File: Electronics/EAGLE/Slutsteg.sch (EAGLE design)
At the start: 151 parts, among them CN1 OSTYK33102030-2, CN2 OSTYK33102030-2, CN3 OSTYK33102030-2, CN4 OSTYK33102030-2, IC1 SPX1117M3-L-3-3_TR, IC10 LM324D, IC11 L78M12ABDT-TR, IC3 ESP32-WROVER-IE-4MB, IC4 TM8211, IC6 TPA3244DDWR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

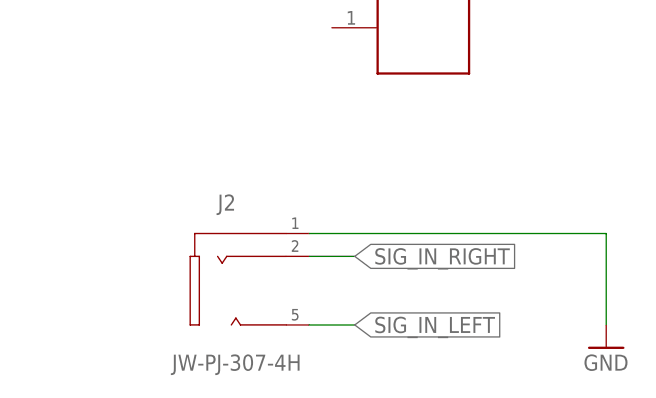
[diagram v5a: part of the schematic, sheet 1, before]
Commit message: Revert "Lagt till 3.5mm connector"
This reverts commit b586c7d4102b99b6a6c1c70b6fd3026c9e3e15a7.
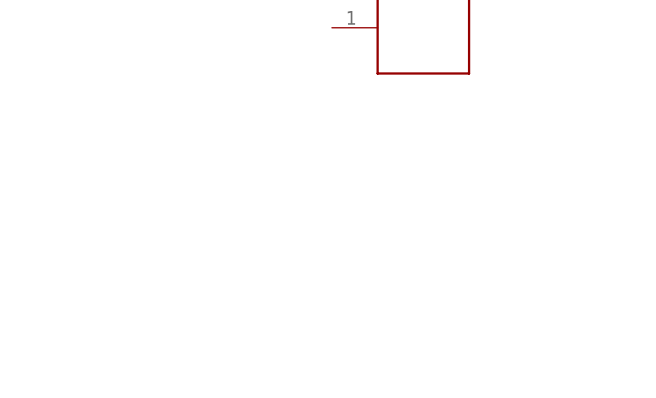
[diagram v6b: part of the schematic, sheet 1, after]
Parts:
- removed J2: JW-PJ-307-4H, jack_04:JW-PJ-307-4H
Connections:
- net GND: no longer J2.1
- net SIG_IN_LEFT: no longer J2.5
- net SIG_IN_RIGHT: no longer J2.2
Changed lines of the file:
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@@
 <part name="C78" library="rcl" library_urn="urn:adsk.eagle:library:334" deviceset="C-EU" device="C0805" package3d_urn="urn:adsk.eagle:package:23617/2" value="1uF/50V"/>
 <part name="C79" library="rcl" library_urn="urn:adsk.eagle:library:334" deviceset="C-EU" device="C0805" package3d_urn="urn:adsk.eagle:package:23617/2" value="1uF/50V"/>
-<part name="J2" library="jack_04" deviceset="JW-PJ-307-4" device="H"/>
-<part name="GND10" library="supply1" library_urn="urn:adsk.eagle:library:371" deviceset="GND" device=""/>
 </parts>
 <sheets>
@@
 <attribute name="VALUE" x="99.06" y="154.94" size="1.778" layer="96"/>
 </instance>
-<instance part="J2" gate="G$1" x="327.66" y="99.06" smashed="yes">
-<attribute name="NAME" x="325.12" y="106.68" size="1.778" layer="95"/>
-<attribute name="VALUE" x="320.04" y="88.9" size="1.778" layer="96"/>
-</instance>
-<instance part="GND10" gate="1" x="368.3" y="91.44" smashed="yes">
-<attribute name="VALUE" x="365.76" y="88.9" size="1.778" layer="96"/>
-</instance>
 </instances>
 <busses>
@@
 <wire x1="101.6" y1="160.02" x2="101.6" y2="198.12" width="0.1524" layer="91"/>
 <wire x1="101.6" y1="198.12" x2="111.76" y2="198.12" width="0.1524" layer="91"/>
-</segment>
-<segment>
-<pinref part="GND10" gate="1" pin="GND"/>
-<pinref part="J2" gate="G$1" pin="1"/>
-<wire x1="368.3" y1="93.98" x2="368.3" y2="104.14" width="0.1524" layer="91"/>
-<wire x1="368.3" y1="104.14" x2="335.28" y2="104.14" width="0.1524" layer="91"/>
 </segment>
 </net>
@@
 </segment>
 </net>
-<net name="SIG_IN_RIGHT" class="0">
-<segment>
-<pinref part="J2" gate="G$1" pin="2"/>
-<wire x1="335.28" y1="101.6" x2="340.36" y2="101.6" width="0.1524" layer="91"/>
-<label x="340.36" y="101.6" size="1.778" layer="95" xref="yes"/>
-</segment>
-</net>
-<net name="SIG_IN_LEFT" class="0">
-<segment>
-<pinref part="J2" gate="G$1" pin="5"/>
-<wire x1="335.28" y1="93.98" x2="340.36" y2="93.98" width="0.1524" layer="91"/>
-<label x="340.36" y="93.98" size="1.778" layer="95" xref="yes"/>
-</segment>
-</net>

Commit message: Changed components
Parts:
- C18: value ECA-1HM471B -> 16PK470MEFC8X11.5; device SamacSys_Parts:ECA-1HM471B -> SamacSys_Parts:16PK470MEFC8X11.5
- C30, C31: device SamacSys_Parts:ECA-1HM471B -> SamacSys_Parts:UVY1H102MHD
- C47: device TPA3244.dbl:SAMACSYS_PARTS_ECA-1HM471B -> SamacSys_Parts:16PK470MEFC8X11.5
- C63, C64: device TPA3244.dbl:SAMACSYS_PARTS_ECA-1HM471B -> SamacSys_Parts:UVY1H102MHD
- L1, L2, L3, L4: value 74477010 -> 48100SC; device SamacSys_Parts:74477010 -> SamacSys_Parts:48100SC
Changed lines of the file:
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@@
 <part name="FRAME1" library="frames" library_urn="urn:adsk.eagle:library:229" deviceset="A3L-LOC" device=""/>
 <part name="IC7" library="SamacSys_Parts" deviceset="TPA3251D2DDVR" device=""/>
-<part name="C63" library="TPA3244.dbl" deviceset="SAMACSYS_PARTS_ECA-1HM471B" device="" value="ECA-1HM102B"/>
-<part name="C64" library="TPA3244.dbl" deviceset="SAMACSYS_PARTS_ECA-1HM471B" device="" value="ECA-1HM102B"/>
+<part name="C63" library="SamacSys_Parts" deviceset="UVY1H102MHD" device="" value="ECA-1HM102B"/>
+<part name="C64" library="SamacSys_Parts" deviceset="UVY1H102MHD" device="" value="ECA-1HM102B"/>
 <part name="L5" library="SamacSys_Parts" deviceset="74477010" device=""/>
 <part name="L6" library="SamacSys_Parts" deviceset="74477010" device=""/>
@@
 <part name="C59" library="rcl" library_urn="urn:adsk.eagle:library:334" deviceset="C-EU" device="C0805" package3d_urn="urn:adsk.eagle:package:23617/2" value="1uF/50V"/>
 <part name="C52" library="rcl" library_urn="urn:adsk.eagle:library:334" deviceset="C-EU" device="C0603" package3d_urn="urn:adsk.eagle:package:23616/2" value="100nF/50V"/>
-<part name="C47" library="TPA3244.dbl" deviceset="SAMACSYS_PARTS_ECA-1HM471B" device="" value="ECA-1HM471B"/>
+<part name="C47" library="SamacSys_Parts" deviceset="16PK470MEFC8X11.5" device="" value="ECA-1HM471B"/>
 <part name="C53" library="rcl" library_urn="urn:adsk.eagle:library:334" deviceset="C-EU" device="C0603" package3d_urn="urn:adsk.eagle:package:23616/2" value="100nF/50V"/>
 <part name="C51" library="rcl" library_urn="urn:adsk.eagle:library:334" deviceset="C-EU" device="C0603" package3d_urn="urn:adsk.eagle:package:23616/2" value="100nF/50V"/>
@@
 <part name="C44" library="rcl" library_urn="urn:adsk.eagle:library:334" deviceset="C-EU" device="C0603" package3d_urn="urn:adsk.eagle:package:23616/2" value="10nF/50V"/>
 <part name="R22" library="rcl" library_urn="urn:adsk.eagle:library:334" deviceset="R-EU_" device="R0603" package3d_urn="urn:adsk.eagle:package:23555/3" value="3.3R/5%/0.1W"/>
-<part name="C31" library="SamacSys_Parts" deviceset="ECA-1HM471B" device="" override_package3d_urn="urn:adsk.eagle:package:27155028/2" override_package_urn="urn:adsk.eagle:footprint:27155054/1" value="ECA-1HM102B"/>
-<part name="C30" library="SamacSys_Parts" deviceset="ECA-1HM471B" device="" override_package3d_urn="urn:adsk.eagle:package:27154914/2" override_package_urn="urn:adsk.eagle:footprint:27154916/1" value="ECA-1HM102B"/>
+<part name="C31" library="SamacSys_Parts" deviceset="UVY1H102MHD" device="" override_package3d_urn="urn:adsk.eagle:package:27155028/2" override_package_urn="urn:adsk.eagle:footprint:27155054/1" override_locally_modified="yes" value="ECA-1HM102B"/>
+<part name="C30" library="SamacSys_Parts" deviceset="UVY1H102MHD" device="" override_package3d_urn="urn:adsk.eagle:package:27154914/2" override_package_urn="urn:adsk.eagle:footprint:27154916/1" override_locally_modified="yes" value="ECA-1HM102B"/>
 <part name="R17" library="rcl" library_urn="urn:adsk.eagle:library:334" deviceset="R-EU_" device="R0603" package3d_urn="urn:adsk.eagle:package:23555/3" value="20K/5%/0.1W"/>
 <part name="C16" library="rcl" library_urn="urn:adsk.eagle:library:334" deviceset="C-EU" device="C0603" package3d_urn="urn:adsk.eagle:package:23616/2" value="100nF/50V"/>
@@
 <part name="C26" library="rcl" library_urn="urn:adsk.eagle:library:334" deviceset="C-EU" device="C0603" package3d_urn="urn:adsk.eagle:package:23616/2" value="100nF/50V"/>
 <part name="R18" library="rcl" library_urn="urn:adsk.eagle:library:334" deviceset="R-EU_" device="R0603" package3d_urn="urn:adsk.eagle:package:23555/3" value="3.3R/5%/0.1W"/>
-<part name="C18" library="SamacSys_Parts" deviceset="ECA-1HM471B" device="" override_package3d_urn="urn:adsk.eagle:package:27158126/2" override_package_urn="urn:adsk.eagle:footprint:27158127/1"/>
+<part name="C18" library="SamacSys_Parts" deviceset="16PK470MEFC8X11.5" device="" override_package3d_urn="urn:adsk.eagle:package:27158126/2" override_package_urn="urn:adsk.eagle:footprint:27158127/1" override_locally_modified="yes"/>
 <part name="C19" library="rcl" library_urn="urn:adsk.eagle:library:334" deviceset="C-EU" device="C0603" package3d_urn="urn:adsk.eagle:package:23616/2" value="100nF/50V"/>
 <part name="R16" library="rcl" library_urn="urn:adsk.eagle:library:334" deviceset="R-EU_" device="R0603" package3d_urn="urn:adsk.eagle:package:23555/3" value="20K/5%/0.1W"/>
@@
 <part name="R12" library="rcl" library_urn="urn:adsk.eagle:library:334" deviceset="R-EU_" device="R0603" package3d_urn="urn:adsk.eagle:package:23555/3" value="20K/5%/0.1W"/>
 <part name="+3V8" library="supply1" library_urn="urn:adsk.eagle:library:371" deviceset="+3V3" device=""/>
-<part name="L1" library="SamacSys_Parts" deviceset="74477010" device="" override_package3d_urn="urn:adsk.eagle:package:27154887/2" override_package_urn="urn:adsk.eagle:footprint:27154892/1"/>
-<part name="L2" library="SamacSys_Parts" deviceset="74477010" device="" override_package3d_urn="urn:adsk.eagle:package:27154899/2" override_package_urn="urn:adsk.eagle:footprint:27154900/1"/>
-<part name="L3" library="SamacSys_Parts" deviceset="74477010" device="" override_package3d_urn="urn:adsk.eagle:package:27154902/2" override_package_urn="urn:adsk.eagle:footprint:27154903/1"/>
-<part name="L4" library="SamacSys_Parts" deviceset="74477010" device="" override_package3d_urn="urn:adsk.eagle:package:27154904/2" override_package_urn="urn:adsk.eagle:footprint:27154905/1"/>
+<part name="L1" library="SamacSys_Parts" deviceset="48100SC" device="" override_package3d_urn="urn:adsk.eagle:package:27154887/2" override_package_urn="urn:adsk.eagle:footprint:27154892/1" override_locally_modified="yes"/>
+<part name="L2" library="SamacSys_Parts" deviceset="48100SC" device="" override_package3d_urn="urn:adsk.eagle:package:27154899/2" override_package_urn="urn:adsk.eagle:footprint:27154900/1" override_locally_modified="yes"/>
+<part name="L3" library="SamacSys_Parts" deviceset="48100SC" device="" override_package3d_urn="urn:adsk.eagle:package:27154902/2" override_package_urn="urn:adsk.eagle:footprint:27154903/1" override_locally_modified="yes"/>
+<part name="L4" library="SamacSys_Parts" deviceset="48100SC" device="" override_package3d_urn="urn:adsk.eagle:package:27154904/2" override_package_urn="urn:adsk.eagle:footprint:27154905/1" override_locally_modified="yes"/>
 <part name="C20" library="rcl" library_urn="urn:adsk.eagle:library:334" deviceset="C-EU" device="C0805" package3d_urn="urn:adsk.eagle:package:23617/2" value="1uF/50V"/>
 <part name="C23" library="rcl" library_urn="urn:adsk.eagle:library:334" deviceset="C-EU" device="C0805" package3d_urn="urn:adsk.eagle:package:23617/2" value="1uF/50V"/>
@@
 <segment>
 <pinref part="IC6" gate="G$1" pin="!RESET"/>
-<wire x1="152.4" y1="162.56" x2="71.12" y2="162.56" width="0.1524" layer="91"/>
+<wire x1="152.4" y1="162.56" x2="76.2" y2="162.56" width="0.1524" layer="91"/>
 <label x="71.12" y="162.56" size="0.8128" layer="95" rot="R180" xref="yes"/>
 <pinref part="R12" gate="G$1" pin="1"/>
-<wire x1="76.2" y1="175.26" x2="71.12" y2="162.56" width="0.1524" layer="91"/>
-<junction x="71.12" y="162.56"/>
-</segment>
-</net>
+<wire x1="76.2" y1="175.26" x2="76.2" y2="162.56" width="0.1524" layer="91"/>
+<junction x="76.2" y="162.56"/>
+<wire x1="76.2" y1="162.56" x2="71.12" y2="162.56" width="0.1524" layer="91"/>
+</segment>
+</net>

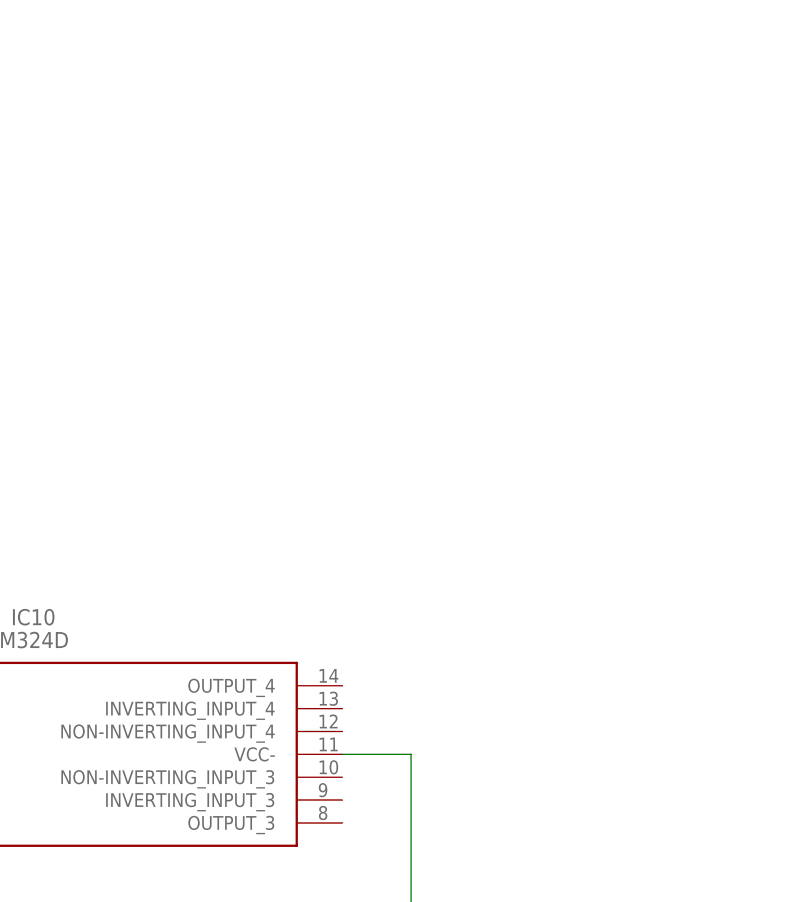
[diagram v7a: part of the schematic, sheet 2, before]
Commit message: Lagt till 3.5mm input och vridpot för Basen
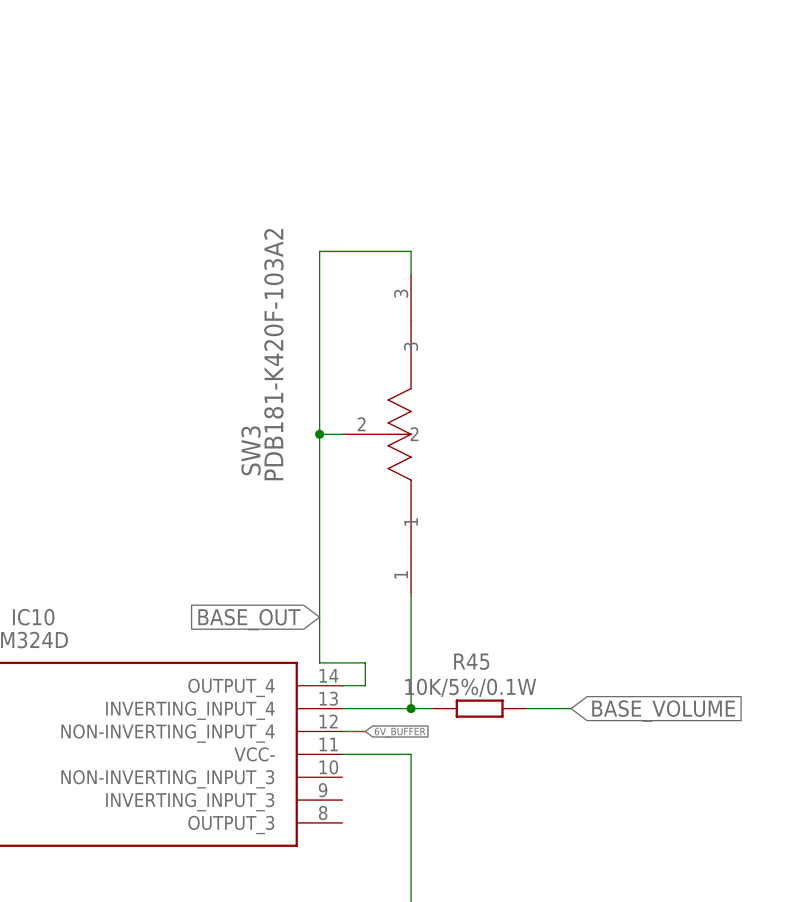
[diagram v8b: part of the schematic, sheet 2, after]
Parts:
- added J2: JW-PJ-307-4H, jack_04:JW-PJ-307-4H
- added R45: 10K/5%/0.1W, rcl:R-EU_R0603
- added SW3: PDB181-K420F-103A2, PDB181-K420F-103A2:PDB181-K420F-103A2
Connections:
- new net N$4: IC10.INVERTING_INPUT_4, R45.2, SW3.1
- net 6V_BUFFER: now also IC10.NON-INVERTING_INPUT_4
- net BASE_OUT: now also IC10.OUTPUT_4, SW3.2, SW3.3; no longer C75.1, R33.1
- net BASE_VOLUME: now also C75.1, R33.1, R45.1
- net GND: now also J2.1
- net SIG_IN_LEFT: now also J2.5
- net SIG_IN_RIGHT: now also J2.2
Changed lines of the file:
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@@
 <part name="C78" library="rcl" library_urn="urn:adsk.eagle:library:334" deviceset="C-EU" device="C0805" package3d_urn="urn:adsk.eagle:package:23617/2" value="1uF/50V"/>
 <part name="C79" library="rcl" library_urn="urn:adsk.eagle:library:334" deviceset="C-EU" device="C0805" package3d_urn="urn:adsk.eagle:package:23617/2" value="1uF/50V"/>
+<part name="J2" library="jack_04" deviceset="JW-PJ-307-4" device="H"/>
+<part name="GND10" library="supply1" library_urn="urn:adsk.eagle:library:371" deviceset="GND" device=""/>
+<part name="SW3" library="PDB181-K420F-103A2" deviceset="PDB181-K420F-103A2" device=""/>
+<part name="R45" library="rcl" library_urn="urn:adsk.eagle:library:334" deviceset="R-EU_" device="R0603" package3d_urn="urn:adsk.eagle:package:23555/3" value="10K/5%/0.1W"/>
 </parts>
 <sheets>
@@
 <attribute name="VALUE" x="99.06" y="154.94" size="1.778" layer="96"/>
 </instance>
+<instance part="J2" gate="G$1" x="325.12" y="68.58" smashed="yes">
+<attribute name="NAME" x="322.58" y="76.2" size="1.778" layer="95"/>
+<attribute name="VALUE" x="317.5" y="58.42" size="1.778" layer="96"/>
+</instance>
+<instance part="GND10" gate="1" x="365.76" y="60.96" smashed="yes">
+<attribute name="VALUE" x="363.22" y="58.42" size="1.778" layer="96"/>
+</instance>
 </instances>
 <busses>
@@
 <wire x1="101.6" y1="160.02" x2="101.6" y2="198.12" width="0.1524" layer="91"/>
 <wire x1="101.6" y1="198.12" x2="111.76" y2="198.12" width="0.1524" layer="91"/>
+</segment>
+<segment>
+<pinref part="GND10" gate="1" pin="GND"/>
+<pinref part="J2" gate="G$1" pin="1"/>
+<wire x1="365.76" y1="63.5" x2="365.76" y2="73.66" width="0.1524" layer="91"/>
+<wire x1="365.76" y1="73.66" x2="332.74" y2="73.66" width="0.1524" layer="91"/>
 </segment>
 </net>
@@
 <wire x1="149.86" y1="198.12" x2="154.94" y2="198.12" width="0.1524" layer="91"/>
 <junction x="149.86" y="198.12"/>
+</segment>
+</net>
+<net name="SIG_IN_RIGHT" class="0">
+<segment>
+<pinref part="J2" gate="G$1" pin="2"/>
+<wire x1="332.74" y1="71.12" x2="337.82" y2="71.12" width="0.1524" layer="91"/>
+<label x="337.82" y="71.12" size="1.778" layer="95" xref="yes"/>
+</segment>
+</net>
+<net name="SIG_IN_LEFT" class="0">
+<segment>
+<pinref part="J2" gate="G$1" pin="5"/>
+<wire x1="332.74" y1="63.5" x2="337.82" y2="63.5" width="0.1524" layer="91"/>
+<label x="337.82" y="63.5" size="1.778" layer="95" xref="yes"/>
 </segment>
 </net>
@@
 <instance part="GND9" gate="1" x="370.84" y="33.02" smashed="yes" rot="MR0">
 <attribute name="VALUE" x="373.38" y="30.48" size="1.778" layer="96" rot="MR0"/>
+</instance>
+<instance part="SW3" gate="A" x="370.84" y="106.68" smashed="yes" rot="R90">
+<attribute name="NAME" x="354.1014" y="122.2756" size="2.0828" layer="95" ratio="6" rot="SR90"/>
+<attribute name="VALUE" x="356.6414" y="121.6406" size="2.0828" layer="96" ratio="6" rot="SR90"/>
+</instance>
+<instance part="R45" gate="G$1" x="378.46" y="96.52" smashed="yes" rot="R180">
+<attribute name="NAME" x="379.73" y="102.6414" size="1.778" layer="95" rot="R180"/>
+<attribute name="VALUE" x="384.81" y="99.822" size="1.778" layer="96" rot="R180"/>
 </instance>
 </instances>
@@
 <wire x1="116.84" y1="88.9" x2="119.38" y2="88.9" width="0.1524" layer="91" style="longdash"/>
 <label x="119.38" y="88.9" size="0.8128" layer="95" xref="yes"/>
+</segment>
+</net>
+<net name="6V_BUFFER" class="0">
+<segment>
+<pinref part="IC10" gate="G$1" pin="NON-INVERTING_INPUT_4"/>
+<wire x1="363.22" y1="93.98" x2="365.76" y2="93.98" width="0.1524" layer="91"/>
+<label x="365.76" y="93.98" size="0.8128" layer="95" xref="yes"/>
+</segment>
+</net>
+<net name="N$4" class="0">
+<segment>
+<pinref part="R45" gate="G$1" pin="2"/>
+<pinref part="IC10" gate="G$1" pin="INVERTING_INPUT_4"/>
+<wire x1="373.38" y1="96.52" x2="370.84" y2="96.52" width="0.1524" layer="91"/>
+<pinref part="SW3" gate="A" pin="1"/>
+<wire x1="370.84" y1="96.52" x2="363.22" y2="96.52" width="0.1524" layer="91"/>
+<wire x1="370.84" y1="109.22" x2="370.84" y2="96.52" width="0.1524" layer="91"/>
+<junction x="370.84" y="96.52"/>
+</segment>
+</net>
+<net name="BASE_OUT" class="0">
+<segment>
+<pinref part="SW3" gate="A" pin="3"/>
+<wire x1="370.84" y1="144.78" x2="370.84" y2="147.32" width="0.1524" layer="91"/>
+<wire x1="370.84" y1="147.32" x2="360.68" y2="147.32" width="0.1524" layer="91"/>
+<wire x1="360.68" y1="147.32" x2="360.68" y2="127" width="0.1524" layer="91"/>
+<wire x1="360.68" y1="127" x2="360.68" y2="101.6" width="0.1524" layer="91"/>
+<wire x1="360.68" y1="101.6" x2="365.76" y2="101.6" width="0.1524" layer="91"/>
+<pinref part="IC10" gate="G$1" pin="OUTPUT_4"/>
+<wire x1="365.76" y1="101.6" x2="365.76" y2="99.06" width="0.1524" layer="91"/>
+<wire x1="365.76" y1="99.06" x2="363.22" y2="99.06" width="0.1524" layer="91"/>
+<label x="360.68" y="106.68" size="1.778" layer="95" rot="R180" xref="yes"/>
+<pinref part="SW3" gate="A" pin="2"/>
+<wire x1="363.22" y1="127" x2="360.68" y2="127" width="0.1524" layer="91"/>
+<junction x="360.68" y="127"/>
+</segment>
+</net>
+<net name="BASE_VOLUME" class="0">
+<segment>
+<pinref part="R45" gate="G$1" pin="1"/>
+<wire x1="383.54" y1="96.52" x2="388.62" y2="96.52" width="0.1524" layer="91"/>
+<label x="388.62" y="96.52" size="1.778" layer="95" xref="yes"/>
 </segment>
 </net>
@@
 </segment>
 </net>
-<net name="BASE_OUT" class="0">
-<segment>
+<net name="BASE_VOLUME" class="0">
+<segment>
+<pinref part="IC9" gate="G$1" pin="OUTPUT_2"/>
+<label x="132.08" y="91.44" size="1.778" layer="95" xref="yes"/>
+<wire x1="172.72" y1="66.04" x2="132.08" y2="66.04" width="0.1524" layer="91"/>
+<wire x1="132.08" y1="66.04" x2="132.08" y2="91.44" width="0.1524" layer="91"/>
 <pinref part="R33" gate="G$1" pin="1"/>
-<wire x1="93.98" y1="86.36" x2="93.98" y2="88.9" width="0.1524" layer="91"/>
+<wire x1="93.98" y1="86.36" x2="93.98" y2="91.44" width="0.1524" layer="91"/>
 <pinref part="C75" gate="G$1" pin="1"/>
-<wire x1="93.98" y1="88.9" x2="116.84" y2="88.9" width="0.1524" layer="91"/>
-<wire x1="116.84" y1="88.9" x2="116.84" y2="86.36" width="0.1524" layer="91"/>
-<wire x1="116.84" y1="88.9" x2="121.92" y2="88.9" width="0.1524" layer="91"/>
-<junction x="116.84" y="88.9"/>
-<label x="121.92" y="88.9" size="1.778" layer="95" xref="yes"/>
-</segment>
-</net>
-<net name="BASE_VOLUME" class="0">
-<segment>
-<pinref part="IC9" gate="G$1" pin="OUTPUT_2"/>
-<wire x1="172.72" y1="66.04" x2="170.18" y2="66.04" width="0.1524" layer="91"/>
-<label x="172.72" y="66.04" size="1.778" layer="95" rot="R180" xref="yes"/>
-</segment>
-</net>
+<wire x1="93.98" y1="91.44" x2="116.84" y2="91.44" width="0.1524" layer="91"/>
+<wire x1="116.84" y1="91.44" x2="116.84" y2="86.36" width="0.1524" layer="91"/>
+<wire x1="132.08" y1="91.44" x2="116.84" y2="91.44" width="0.1524" layer="91"/>
+<junction x="116.84" y="91.44"/>
+</segment>
+</net>
